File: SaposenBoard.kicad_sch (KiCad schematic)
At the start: 82 parts, among them IC1 BSO220, IC2 BSO220, IC3 BSO220, IC4 BSO220, J1 ADC2, J2 I2C, J3 ADC, J4 Encoder1, J5 Encoder2, J6 Motor1, J7 Motor2, J8 Battery, Q1 BSS138, Q2 BSS138, Q3 BSS138, Q4 BSS138, Q5 BSS138, Q6 BSS138, Q7 BSS138, SW1 RESET, SW2 SW, SW3 BatterySW, U1 74CBTLV3257, U4 A4955GLPTR-T, U5 A4955GLPTR-T, U6 NUCLEO-F303K8, U7 MPU-6500

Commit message: [update]部品置いた
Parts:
- removed C3: 0.1u, Capacitor_SMD:C_0603_1608Metric, symbol Device:C
- removed J1: ADC2, Connector_PinHeader_2.54mm:PinHeader_1x04_P2.54mm_Vertical, symbol Connector_Generic:Conn_01x04
- removed J3: ADC, symbol Connector_Generic:Conn_02x05_Counter_Clockwise
- removed R6: 470, Resistor_SMD:R_0603_1608Metric, symbol Device:R
- removed SW1: RESET, Footprints:TVDT18-050C, symbol Switch:SW_Push
- added J1: ADC, Connector_Molex:Molex_Micro-Latch_53253-0670_1x06_P2.00mm_Vertical, symbol Connector_Generic:Conn_01x06
- added J2: ADC/Servo, Connector_PinHeader_2.54mm:PinHeader_2x03_P2.54mm_Vertical, symbol Connector_Generic:Conn_02x03_Odd_Even
- added J4: ADC_Extend, Connector_Molex:Molex_Micro-Latch_53253-0470_1x04_P2.00mm_Vertical, symbol Connector_Generic:Conn_01x04
- U1: footprint (none) -> Package_SO:TSSOP-16_4.4x5mm_P0.65mm
- U2, U3: footprint (none) -> Package_TO_SOT_SMD:SOT-363_SC-70-6
- renumbered J2 to J3, J4 to J5, J5 to J6, J6 to J7, J7 to J8, J8 to J9, R2 to R1, R11 to R10, R12 to R11, R13 to R12, R14 to R13, R15 to R14, R16 to R15, R17 to R16, R18 to R17, R1 to R18, R3 to R2, R4 to R3, R5 to R4, R7 to R6, R8 to R7, R9 to R8, R10 to R9
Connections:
- net +3V3: now also J1.6 (Pin_6), J2.3 (Pin_3), J2.4 (Pin_4)
- net ADC2_1: now also U6.4_6 (PA_7), J2.2 (Pin_2); no longer U6.4_7 (PA_6)
- net ADC2_2: now also U6.4_7 (PA_6), J2.1 (Pin_1); no longer U6.4_8 (PA_5)
- net ENC1_1: now also U6.3_14 (PB_5); no longer U6.3_1 (PA_9)
- net ENC1_2: now also U6.3_15 (PB_4); no longer U6.3_12 (PA_8)
- net ENC2_1: now also U6.3_1 (PA_9); no longer U6.3_14 (PB_5)
- net ENC2_2: now also U6.3_12 (PA_8); no longer U6.3_15 (PB_4)
- net GND: now also J1.1 (Pin_1), J2.5 (Pin_5), J2.6 (Pin_6)
- net MOT2_PH: now also U6.4_8 (PA_5); no longer U6.4_6 (PA_7)
- net Sensor1_1: now reaches U1.2
- net Sensor1_1: now also J1.5 (Pin_5)
- net Sensor2_1: now reaches U1.3
- net Sensor2_1: now also J4.4 (Pin_4)
- net Sensor2_3: now reaches U1.13
- net Sensor2_3: now also J4.2 (Pin_2)
- net Sensor1_3: now reaches U1.14
- net Sensor1_3: now also J1.3 (Pin_3)
- net Sensor2_4: now reaches U1.10
- net Sensor2_4: now also J4.1 (Pin_1)
- net Sensor1_4: now reaches U1.11
- net Sensor1_4: now also J1.2 (Pin_2)
- net Sensor1_2: now reaches U1.5
- net Sensor1_2: now also J1.4 (Pin_4)
- net Sensor2_2: now reaches U1.6
- net Sensor2_2: now also J4.3 (Pin_3)
- net NRST: no longer names the net of U6.4_3 (NRST)
- no-connect marks 11 -> 12
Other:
- moved on the sheet: C4, D1, J3, J5, J6, LS1, Q3, Q4, Q5, Q6, Q7, R10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

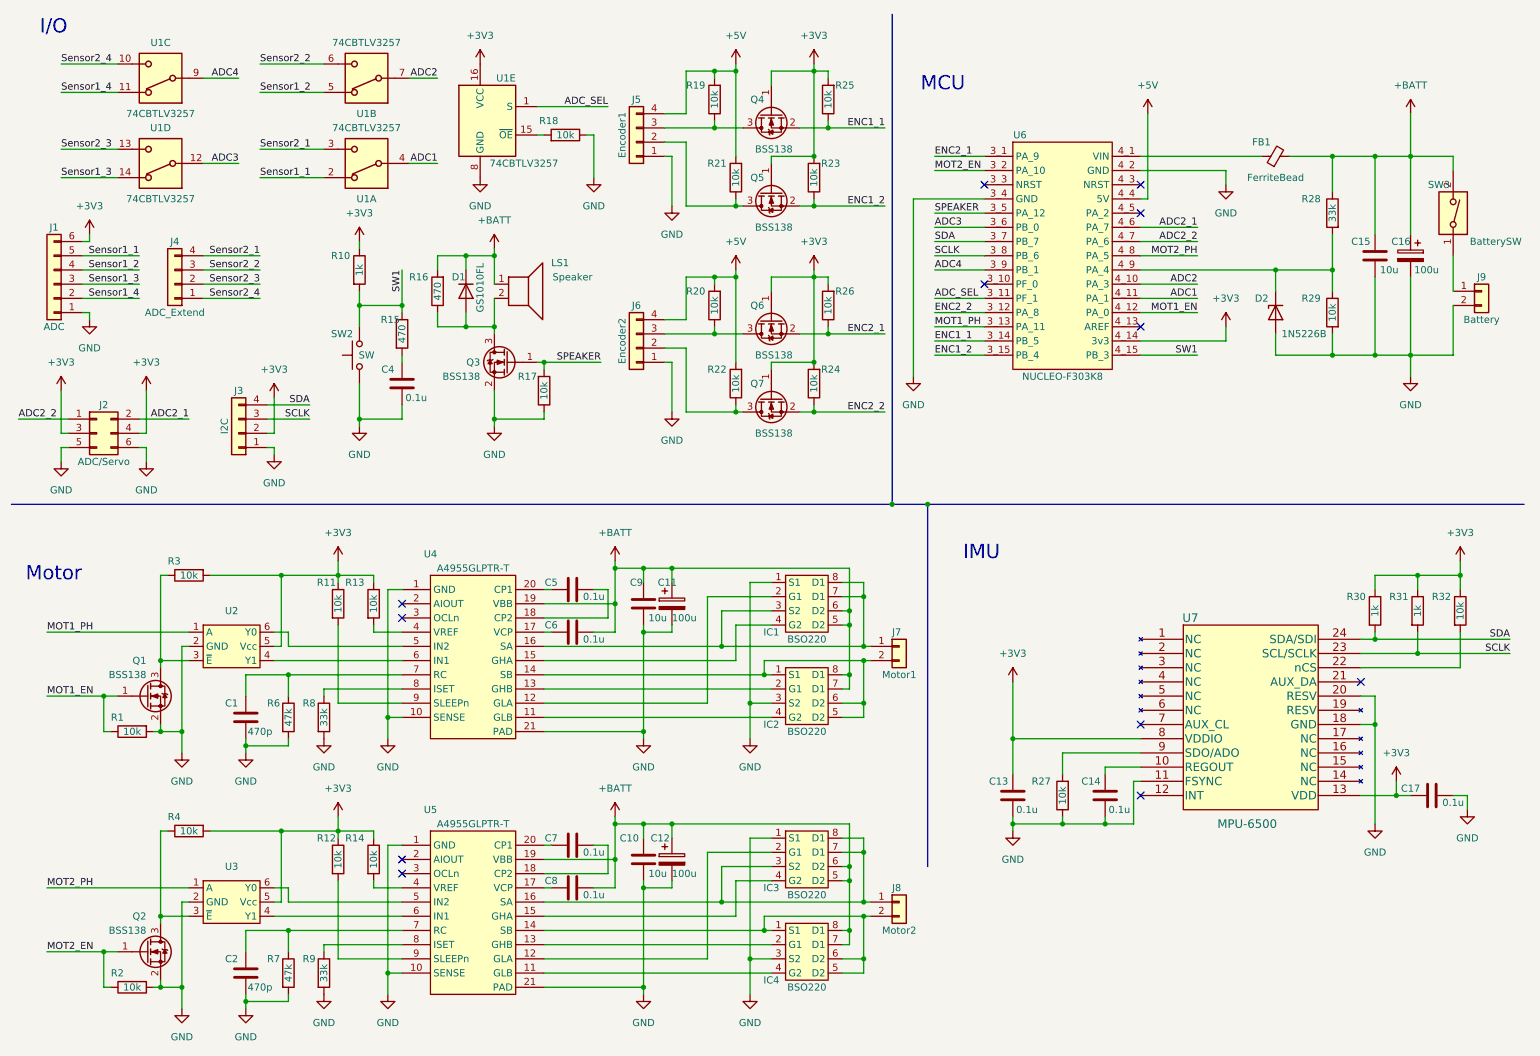
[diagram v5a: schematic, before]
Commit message: [update]フットプリントを調整
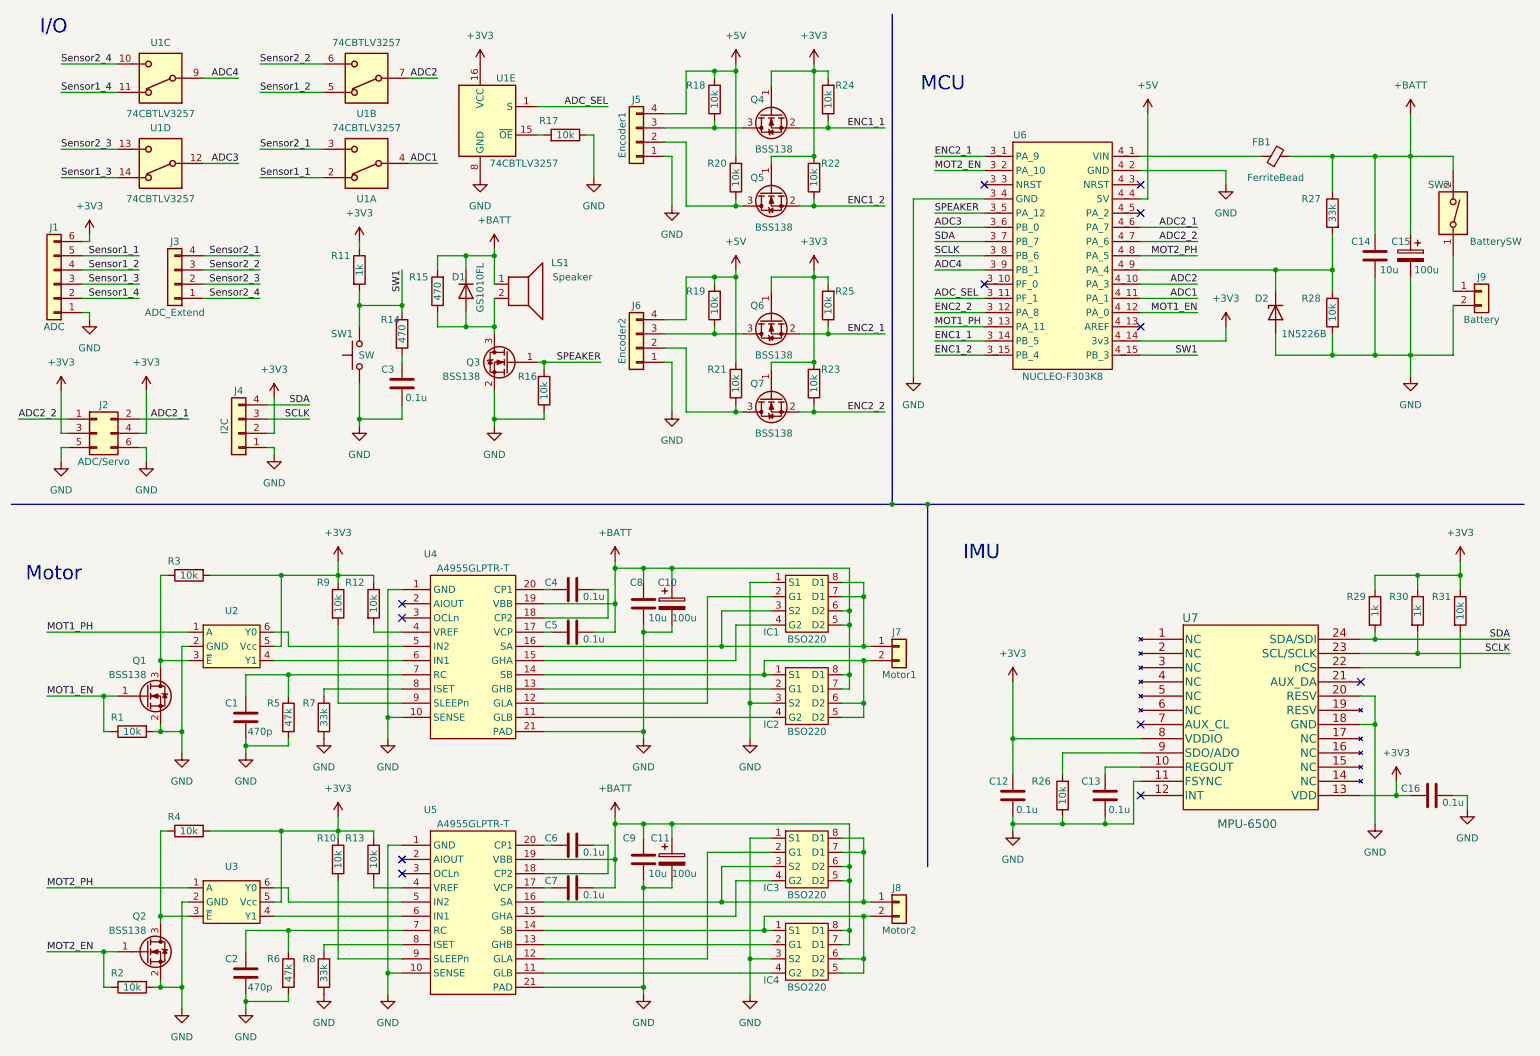
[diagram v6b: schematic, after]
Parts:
- renumbered C11 to C10, C12 to C11, C13 to C12, C14 to C13, C15 to C14, C16 to C15, C17 to C16, C4 to C3, C5 to C4, C6 to C5, C7 to C6, C8 to C7, C9 to C8, C10 to C9, J4 to J3, J3 to J4, R12 to R10, R10 to R11, R13 to R12, R14 to R13, R15 to R14, R16 to R15, R17 to R16, R18 to R17, R19 to R18, R20 to R19, R21 to R20, R22 to R21, R23 to R22, R24 to R23, R25 to R24, R26 to R25, R27 to R26, R28 to R27, R29 to R28, R30 to R29, R31 to R30, R32 to R31, R6 to R5, R7 to R6, R8 to R7, R9 to R8, R11 to R9, SW2 to SW1, SW3 to SW2
